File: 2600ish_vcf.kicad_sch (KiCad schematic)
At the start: 99 parts, among them J1 AUDIO IN 1, J2 AUDIO IN 2, J2 CV 1, J2 CV2, J2 V/OCT IN, J3 OUT, Q1 2N3906, Q10 2N3906, Q11 2N3906, Q12 2N3906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

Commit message: PCB layout started
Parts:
- removed R1 (x2): 100k, Potentiometer_THT:Potentiometer_Alpha_RD901F-40-00D_Single_Vertical, symbol Device:R_Potentiometer
- added P4: 100k, Potentiometer_THT:Potentiometer_Double_Vertical_Befaco, symbol Device:R_Potentiometer_Dual
- C10, C9: footprint (none) -> Capacitor_THT:CP_Radial_D4.0mm_P2.00mm
- Q1, Q10, Q11, Q12, Q2, Q3, Q4, Q5, Q6, Q7, Q8, Q9: footprint Package_TO_SOT_THT:TO-92_Inline -> Package_TO_SOT_THT:TO-92_Wide
- R1: footprint Potentiometer_THT:Potentiometer_Alpha_RD901F-40-00D_Single_Vertical -> Potentiometer_THT:Potentiometer_Bourns_3296W_Vertical
- R16, R19, R2, R3, R5: footprint Resistor_THT:R_Axial_DIN0207_L6.3mm_D2.5mm_P2.54mm_Vertical -> Resistor_THT:R_Axial_DIN0207_L6.3mm_D2.5mm_P7.62mm_Horizontal
- U1, U2: footprint (none) -> Package_DIP:DIP-14_W7.62mm_Socket_LongPads
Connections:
- net GND: now also P4.1, P4.4
- net at R19.2: now also P4.5
- net at C9.1: now also P4.3, P4.6
- net at R5.1: now also P4.2

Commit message: component placement done
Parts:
- removed J2: CV2, Connector_Audio:Jack_3.5mm_QingPu_WQP-PJ398SM_Vertical_CircularHoles, symbol Connector_Audio:AudioJack2_SwitchT
- removed R1: 50K lin, Potentiometer_THT:Potentiometer_Alpha_RD901F-40-00D_Single_Vertical, symbol Device:R_Potentiometer
- removed R19: 100k, Resistor_THT:R_Axial_DIN0207_L6.3mm_D2.5mm_P7.62mm_Horizontal, symbol Device:R
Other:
- note added: "CV2 was here originally too, but arguably not implemented in a modular way"

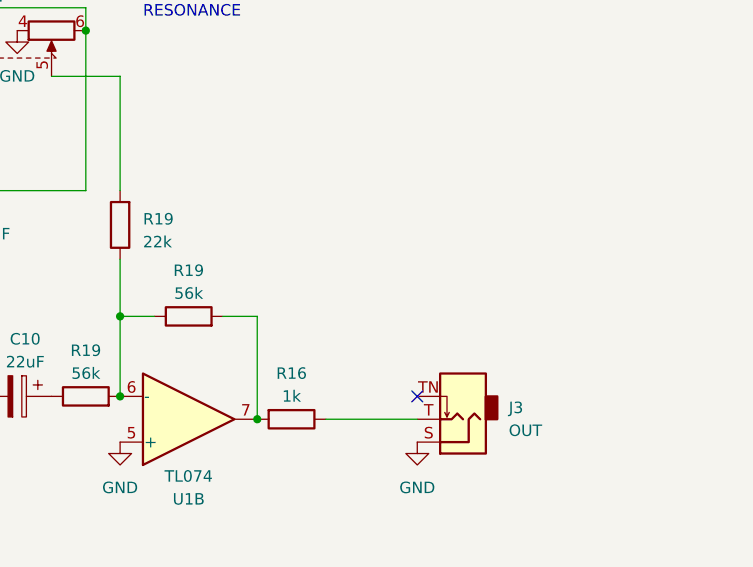
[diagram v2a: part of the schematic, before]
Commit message: Some adjustments made for gain and footprint size
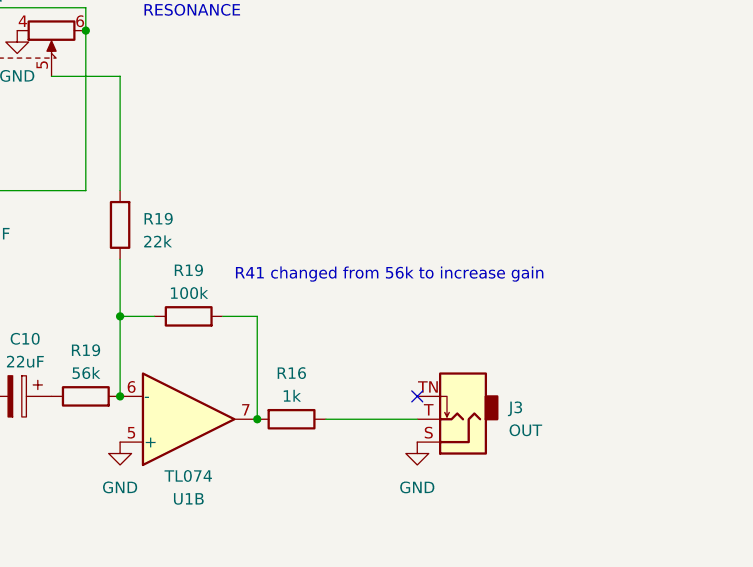
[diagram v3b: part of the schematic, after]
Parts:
- C7: footprint Capacitor_THT:C_Disc_D6.0mm_W2.5mm_P5.00mm -> Capacitor_THT:C_Axial_L5.1mm_D3.1mm_P10.00mm_Horizontal
- R19: value 56k -> 100k
- R5: footprint Resistor_THT:R_Axial_DIN0207_L6.3mm_D2.5mm_P7.62mm_Horizontal -> Resistor_THT:R_Axial_DIN0207_L6.3mm_D2.5mm_P2.54mm_Vertical
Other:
- note added: "R41 changed from 56k to increase gain"
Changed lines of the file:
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@@
     (effects (font (size 1.27 1.27)) (justify left bottom))
   )
+  (text "R41 changed from 56k to increase gain" (at 342.9 52.07 0)
+    (effects (font (size 1.27 1.27)) (justify left bottom))
+  )
   (global_label "+12V" (shape input) (at 91.44 86.36 90) (fields_autoplaced)
     (effects (font (size 1.27 1.27)) (justify left))
@@
       (effects (font (size 1.27 1.27)) (justify right))
     )
-    (property "Footprint" "Resistor_THT:R_Axial_DIN0207_L6.3mm_D2.5mm_P7.62mm_Horizontal" (at 300.228 143.51 90)
+    (property "Footprint" "Resistor_THT:R_Axial_DIN0207_L6.3mm_D2.5mm_P2.54mm_Vertical" (at 300.228 143.51 90)
       (effects (font (size 1.27 1.27)) hide)
     )
@@
       (effects (font (size 1.27 1.27)))
     )
-    (property "Footprint" "Capacitor_THT:C_Disc_D6.0mm_W2.5mm_P5.00mm" (at 335.28 100.6348 0)
+    (property "Footprint" "Capacitor_THT:C_Axial_L5.1mm_D3.1mm_P10.00mm_Horizontal" (at 335.28 100.6348 0)
       (effects (font (size 1.27 1.27)) hide)
     )
@@
       (effects (font (size 1.27 1.27)))
     )
-    (property "Footprint" "Capacitor_THT:C_Disc_D6.0mm_W2.5mm_P5.00mm" (at 234.95 99.3648 0)
+    (property "Footprint" "Capacitor_THT:C_Axial_L5.1mm_D3.1mm_P10.00mm_Horizontal" (at 234.95 99.3648 0)
       (effects (font (size 1.27 1.27)) hide)
     )
@@
       (effects (font (size 1.27 1.27)))
     )
-    (property "Footprint" "Capacitor_THT:C_Disc_D6.0mm_W2.5mm_P5.00mm" (at 285.75 99.3648 0)
+    (property "Footprint" "Capacitor_THT:C_Axial_L5.1mm_D3.1mm_P10.00mm_Horizontal" (at 285.75 99.3648 0)
       (effects (font (size 1.27 1.27)) hide)
     )
@@
       (effects (font (size 1.27 1.27)))
     )
-    (property "Value" "56k" (at 337.82 53.34 90)
+    (property "Value" "100k" (at 337.82 53.34 90)
       (effects (font (size 1.27 1.27)))
     )
@@
       (effects (font (size 1.27 1.27)))
     )
-    (property "Footprint" "Capacitor_THT:C_Disc_D6.0mm_W2.5mm_P5.00mm" (at 184.15 99.3648 0)
+    (property "Footprint" "Capacitor_THT:C_Axial_L5.1mm_D3.1mm_P10.00mm_Horizontal" (at 184.15 99.3648 0)
       (effects (font (size 1.27 1.27)) hide)
     )

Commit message: Clearer schematic
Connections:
- net AUDIOS IN: now reaches R19.1, R19.2, R19.2, TP7.1, U1.2 (-)
- net RESONANCE 1: now reaches Q1.2 (B), R19.2, R5.2, R5.2
- net RESONANCE 3: now reaches C9.1, P4.3, P4.6
- net RESONANCE 2: now reaches P4.5, R19.2
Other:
- note added: "R35 was 10k in order to send -7.5v into pin 12 Adjusted to 18k to make it more like -6v"
- moved on the sheet: J1, J2, R1, R19

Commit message: Schematic for split board done, updating PCB now
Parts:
- added J6: Conn_01x08_Pin, Connector_PinHeader_2.54mm:PinHeader_2x04_P2.54mm_Vertical, symbol Connector:Conn_01x08_Pin
- added J7: Conn_01x08_Socket, Connector_PinSocket_2.54mm:PinSocket_2x04_P2.54mm_Vertical, symbol Connector:Conn_01x08_Socket
- added J8: Conn_01x04_Pin, Connector_PinHeader_2.54mm:PinHeader_1x04_P2.54mm_Vertical, symbol Connector:Conn_01x04_Pin
- added J9: Conn_01x04_Socket, Connector_PinSocket_2.54mm:PinSocket_1x04_P2.54mm_Vertical, symbol Connector:Conn_01x04_Socket
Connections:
- net +12V: now also J8.1 (Pin_1), J9.1 (Pin_1)
- net -12V: now also J8.4 (Pin_4), J9.4 (Pin_4)
- net AUDIOS IN: now also J6.2 (Pin_2), J7.2 (Pin_2)
- net CUTOFF: now also J6.3 (Pin_3), J7.3 (Pin_3)
- net GND: now also J6.1 (Pin_1), J6.8 (Pin_8), J7.1 (Pin_1), J7.8 (Pin_8), J8.2 (Pin_2), J8.3 (Pin_3), J9.2 (Pin_2), J9.3 (Pin_3)
- net RESONANCE 1: now also J6.4 (Pin_4), J7.4 (Pin_4)
- net RESONANCE 2: now also J6.5 (Pin_5), J7.5 (Pin_5)
- net RESONANCE 3: now also J6.6 (Pin_6), J7.6 (Pin_6)
- net AUDIO OUT: now reaches R16.2, R19.2, U1.7
- net AUDIO OUT: now also J6.7 (Pin_7), J7.7 (Pin_7)
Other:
- moved on the sheet: J3, R16

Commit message: Main PCB pretty much done, panel work started
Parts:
- removed J6: Conn_01x08_Pin, Connector_PinHeader_2.54mm:PinHeader_2x04_P2.54mm_Vertical, symbol Connector:Conn_01x08_Pin
- removed J7: Conn_01x08_Socket, Connector_PinSocket_2.54mm:PinSocket_2x04_P2.54mm_Vertical, symbol Connector:Conn_01x08_Socket
- removed J8: Conn_01x04_Pin, Connector_PinHeader_2.54mm:PinHeader_1x04_P2.54mm_Vertical, symbol Connector:Conn_01x04_Pin
- removed J9: Conn_01x04_Socket, Connector_PinSocket_2.54mm:PinSocket_1x04_P2.54mm_Vertical, symbol Connector:Conn_01x04_Socket

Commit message: Schematic issue and related routing fixed and v0.2 created. New gerbers generated
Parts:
- R19: value 18k -> 10k or 18k
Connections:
- net at Q1.3 (C), Q5.2 (B), R19.2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: no longer Q5.1 (E), Q6.1 (E), R19.2, TP7.1
- new net: Q5.1 (E), Q6.1 (E), R19.2, TP7.1
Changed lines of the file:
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@@
   (junction (at 120.65 261.62) (diameter 0) (color 0 0 0 0)
   )
-  (junction (at 161.29 138.43) (diameter 0) (color 0 0 0 0)
-  )
   (junction (at 52.07 254) (diameter 0) (color 0 0 0 0)
   )
   (junction (at 330.2 64.77) (diameter 0) (color 0 0 0 0)
-  )
-  (junction (at 152.4 138.43) (diameter 0) (color 0 0 0 0)
   )
   (junction (at 238.76 116.84) (diameter 0) (color 0 0 0 0)
@@
     (stroke (width 0) (type default))
   )
-  (wire (pts (xy 148.59 138.43) (xy 152.4 138.43))
-    (stroke (width 0) (type default))
-  )
   (wire (pts (xy 351.79 151.13) (xy 351.79 91.44))
     (stroke (width 0) (type default))
@@
     (stroke (width 0) (type default))
   )
-  (wire (pts (xy 148.59 68.58) (xy 148.59 138.43))
+  (wire (pts (xy 148.59 68.58) (xy 148.59 133.35))
     (stroke (width 0) (type default))
   )
@@
     (stroke (width 0) (type default))
   )
-  (wire (pts (xy 152.4 138.43) (xy 161.29 138.43))
+  (wire (pts (xy 148.59 133.35) (xy 161.29 133.35))
     (stroke (width 0) (type default))
   )
@@
       (effects (font (size 1.27 1.27)) (justify left))
     )
-    (property "Value" "18k" (at 241.3 62.865 0)
+    (property "Value" "10k or 18k" (at 241.3 62.865 0)
       (effects (font (size 1.27 1.27)) (justify left))
     )
